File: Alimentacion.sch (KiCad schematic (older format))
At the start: 3 parts

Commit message: version preliminar de la etapa de alimentacion
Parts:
- added C1, C4: 4,7u, symbol C
- added C? (x2): 4u7, symbol C
- added C?: 10u, symbol C
- added D1: LED, symbol LED
- added L?: 4u7, symbol L
- added P1: CONN_01X02, symbol CONN_01X02
- added Q?: NX2301P, symbol NX2301P
- added Q?: BC849, SOT-23, symbol BC849
- added R1, R2: 470, symbol R
- added R? (x2): 10K, symbol R
- added R?: 976K, symbol R
- added R?: 309K, symbol R
- added R?: 47K, symbol R
- added R?: 1K, symbol R
- added U1: MCP73831T, symbol MCP73831T
- added U?: MCP1640, symbol MCP1640
- U2: renamed from U?; footprint SOT-223 -> (none)
- gave numbers to parts that had none: 2
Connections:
- net labels added: +3V3, +5V, V5VBOOST, VBATT, VUSB
- wire segments 8 -> 59
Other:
- moved on the sheet: C2, C3, U2

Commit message: asignacion inicial de huellas
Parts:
- C1, C3, C4: footprint (none) -> Capacitors_SMD:C_1206
- C2: footprint (none) -> Capacitors_SMD:C_0805
- C34, C35, C36: renamed from C?; footprint (none) -> Capacitors_SMD:C_1206
- D1: footprint (none) -> LEDs:LED_0805
- L2: renamed from L?; footprint (none) -> Magneticos:BOURNS_SRN4012T
- P1: footprint (none) -> Connectors_Molex:Molex_PicoBlade_53047-0210_02x1.25mm_Straight
- Q10: renamed from Q?; footprint SOT-23 -> TO_SOT_Packages_SMD:SOT-23
- Q11: renamed from Q?; footprint (none) -> TO_SOT_Packages_SMD:SOT-23
- R1, R2: footprint (none) -> Resistencias:R_0805
- R54, R55, R56, R57, R58, R59: renamed from R?; footprint (none) -> Resistencias:R_0805
- U1: footprint (none) -> TO_SOT_Packages_SMD:SOT-23-5; Fabricante (none) -> MICROCHIP; Provedor (none) -> rs; Ref (none) -> MCP73831T-2ATI/OT; Ref_Proveedor (none) -> 738-6617
- U12: renamed from U?; footprint (none) -> TO_SOT_Packages_SMD:SOT-23-6
- U2: footprint (none) -> TO_SOT_Packages_SMD:SOT-223; Fabricante (none) -> ST; Ref (none) -> LD1117S33TR

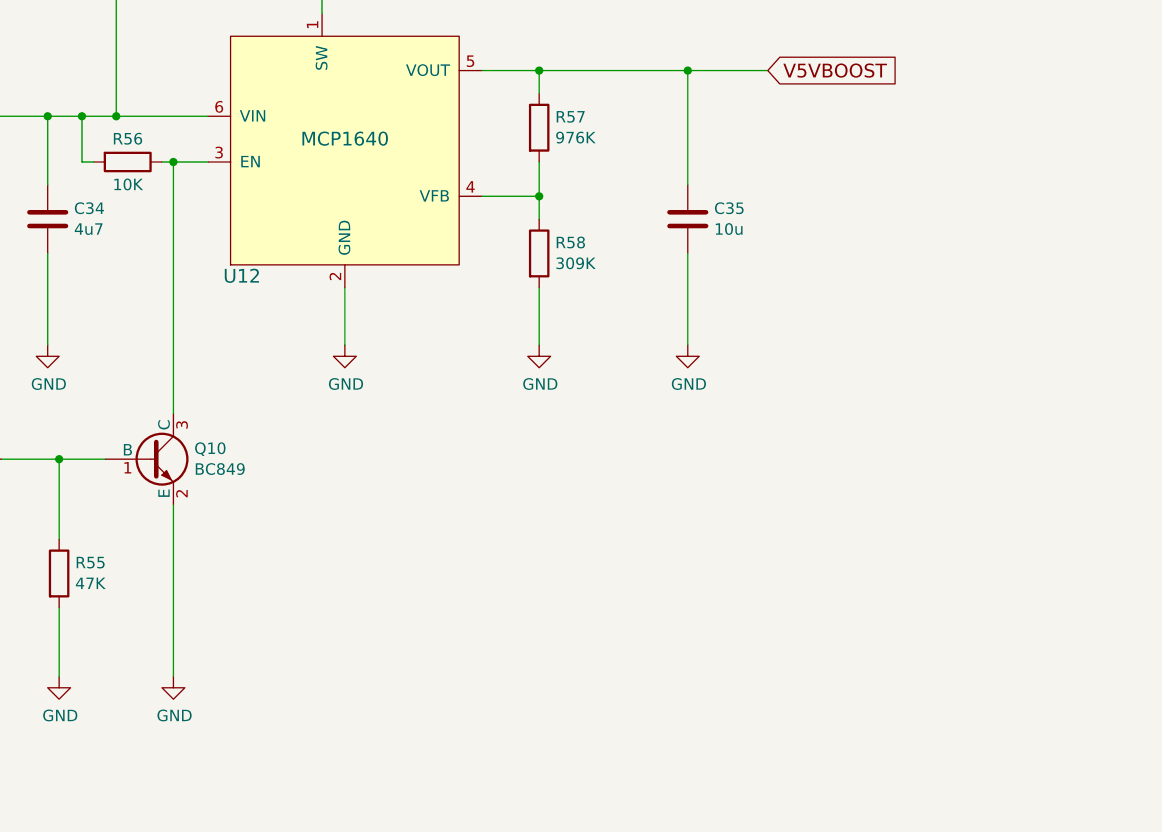
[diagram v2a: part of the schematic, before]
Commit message: cambiar ch340T por ch340g y añadir nc a pines
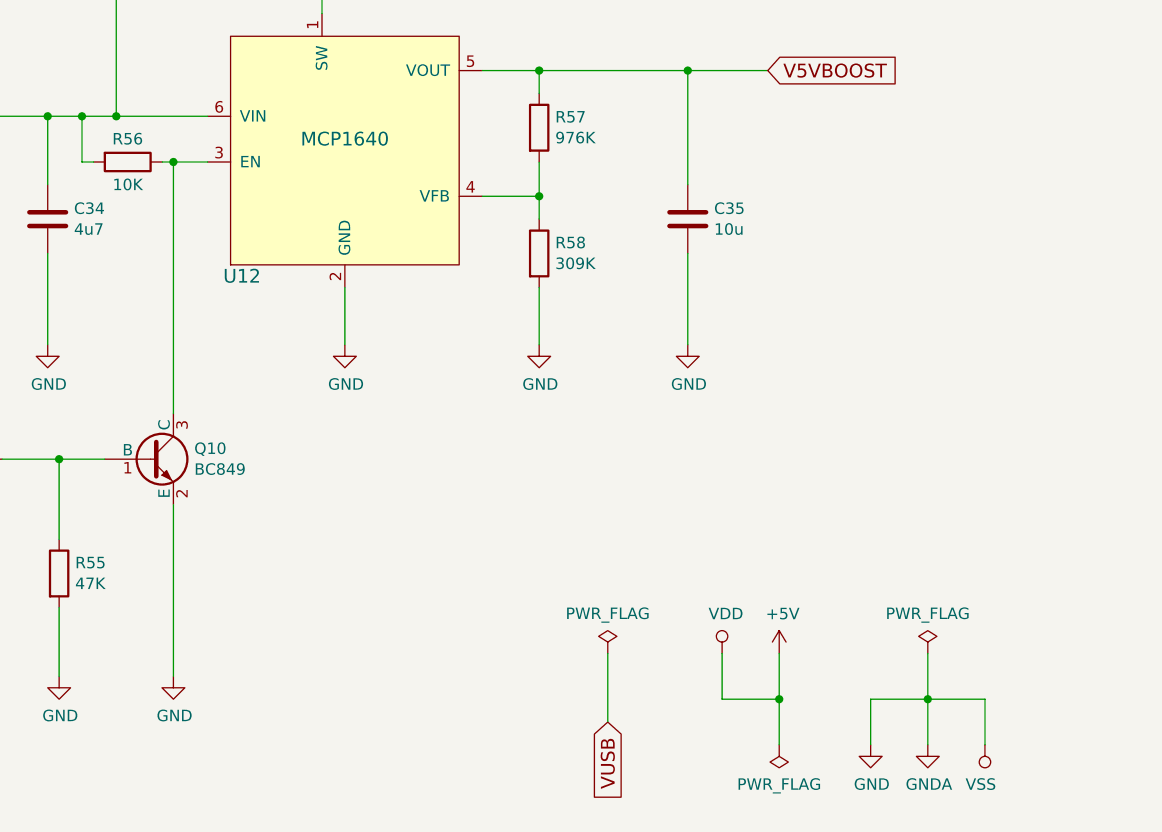
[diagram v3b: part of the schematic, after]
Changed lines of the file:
@@
 $Descr A4 11693 8268
 encoding utf-8
-Sheet 2 15
+Sheet 2 14
 Title "Etapa de Alimentación"
 Date "2017-01-15"
@@
 $EndComp
 Wire Wire Line
-	2900 4450 2700 4450
+	2700 4450 2900 4450
 Wire Wire Line
 	2400 4450 2350 4450
@@
 Wire Wire Line
 	9750 4100 9750 3900
+$Comp
+L PWR_FLAG #FLG016
+U 1 1 589667C8
+P 4650 6600
+F 0 "#FLG016" H 3550 5475 50  0001 C CNN
+F 1 "PWR_FLAG" H 4650 6774 50  0000 C CNN
+F 2 "" H 3550 5400 50  0001 C CNN
+F 3 "" H 3550 5400 50  0001 C CNN
+	1    4650 6600
+	1    0    0    -1
+$EndComp
+Text GLabel 4650 6900 3    60   Input ~ 0
+VUSB
+$Comp
+L +5V #PWR017
+U 1 1 58967CBF
+P 5400 6600
+F 0 "#PWR017" H 5400 6450 50  0001 C CNN
+F 1 "+5V" H 5415 6773 50  0000 C CNN
+F 2 "" H 5400 6600 50  0001 C CNN
+F 3 "" H 5400 6600 50  0001 C CNN
+	1    5400 6600
+	1    0    0    -1
+$EndComp
+$Comp
+L PWR_FLAG #FLG018
+U 1 1 58967D6B
+P 5400 7000
+F 0 "#FLG018" H 4300 5875 50  0001 C CNN
+F 1 "PWR_FLAG" H 5400 7173 50  0000 C CNN
+F 2 "" H 4300 5800 50  0001 C CNN
+F 3 "" H 4300 5800 50  0001 C CNN
+	1    5400 7000
+	-1   0    0    1
+$EndComp
+$Comp
+L GND #PWR019
+U 1 1 58967DD4
+P 5800 7000
+F 0 "#PWR019" H 5850 7050 50  0001 C CNN
+F 1 "GND" H 5805 6827 50  0000 C CNN
+F 2 "" H -100 150 50  0001 C CNN
+F 3 "" H -100 150 50  0001 C CNN
+	1    5800 7000
+	1    0    0    -1
+$EndComp
+$Comp
+L GNDA #PWR020
+U 1 1 58967E16
+P 6050 7000
+F 0 "#PWR020" H 6100 7050 50  0001 C CNN
+F 1 "GNDA" H 6055 6827 50  0000 C CNN
+F 2 "" H 50  0   50  0001 C CNN
+F 3 "" H 50  0   50  0001 C CNN
+	1    6050 7000
+	1    0    0    -1
+$EndComp
+Wire Wire Line
+	6050 6600 6050 7000
+Wire Wire Line
+	5800 6800 6300 6800
+Wire Wire Line
+	5800 6800 5800 7000
+$Comp
+L PWR_FLAG #FLG021
+U 1 1 58967ED4
+P 6050 6600
+F 0 "#FLG021" H 4950 5475 50  0001 C CNN
+F 1 "PWR_FLAG" H 6050 6774 50  0000 C CNN
+F 2 "" H 4950 5400 50  0001 C CNN
+F 3 "" H 4950 5400 50  0001 C CNN
+	1    6050 6600
+	1    0    0    -1
+$EndComp
+Connection ~ 6050 6800
+Wire Wire Line
+	5400 6600 5400 7000
+Wire Wire Line
+	4650 6600 4650 6900
+$Comp
+L VDD #PWR022
+U 1 1 58968AA7
+P 5150 6600
+F 0 "#PWR022" H 5200 6650 50  0001 C CNN
+F 1 "VDD" H 5167 6773 50  0000 C CNN
+F 2 "" H -50 -50 50  0001 C CNN
+F 3 "" H -50 -50 50  0001 C CNN
+	1    5150 6600
+	1    0    0    -1
+$EndComp
+Wire Wire Line
+	5150 6600 5150 6800
+Wire Wire Line
+	5150 6800 5400 6800
+Connection ~ 5400 6800
+$Comp
+L VSS #PWR023
+U 1 1 58968B58
+P 6300 7000
+F 0 "#PWR023" H 6350 7050 50  0001 C CNN
+F 1 "VSS" H 6318 7173 50  0000 C CNN
+F 2 "" H 0   100 50  0001 C CNN
+F 3 "" H 0   100 50  0001 C CNN
+	1    6300 7000
+	-1   0    0    1
+$EndComp
+Wire Wire Line
+	6300 6800 6300 7000
 $EndSCHEMATC

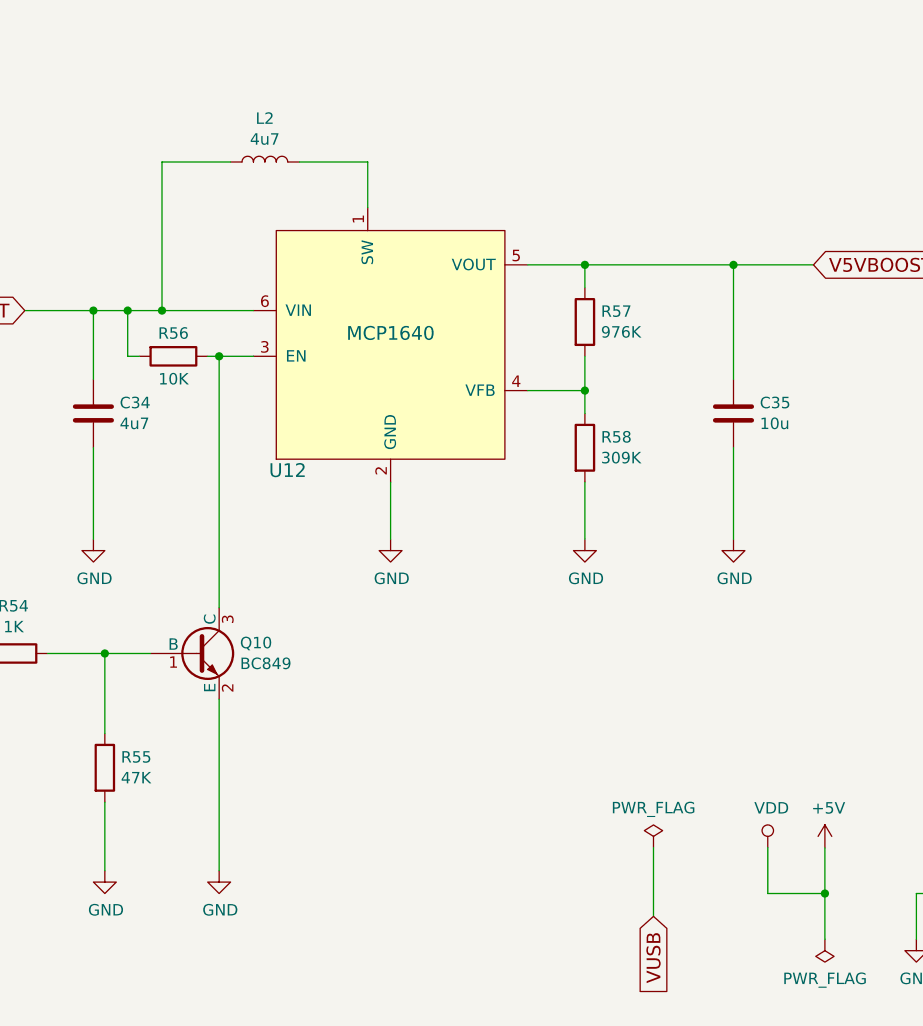
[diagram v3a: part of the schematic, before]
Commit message: cambiado cristal de cuarzo por resonador
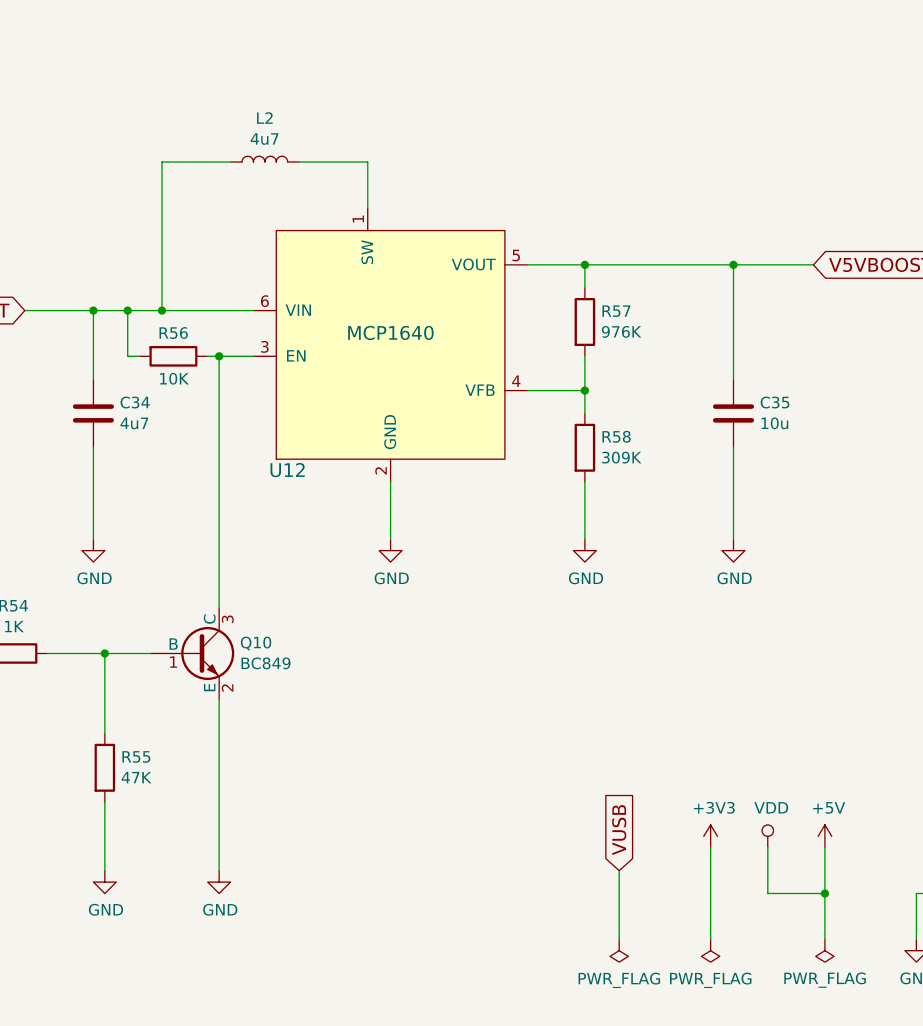
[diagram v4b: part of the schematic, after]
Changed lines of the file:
@@
 	2800 3600 2500 3600
 Wire Wire Line
-	2500 3600 2500 4250
+	2500 4250 2500 3600
 Wire Wire Line
 	1900 4250 2900 4250
@@
 L PWR_FLAG #FLG016
 U 1 1 589667C8
-P 4650 6600
-F 0 "#FLG016" H 3550 5475 50  0001 C CNN
-F 1 "PWR_FLAG" H 4650 6774 50  0000 C CNN
-F 2 "" H 3550 5400 50  0001 C CNN
-F 3 "" H 3550 5400 50  0001 C CNN
-	1    4650 6600
-	1    0    0    -1
-$EndComp
-Text GLabel 4650 6900 3    60   Input ~ 0
+P 4500 7000
+F 0 "#FLG016" H 3400 5875 50  0001 C CNN
+F 1 "PWR_FLAG" H 4500 7174 50  0000 C CNN
+F 2 "" H 3400 5800 50  0001 C CNN
+F 3 "" H 3400 5800 50  0001 C CNN
+	1    4500 7000
+	-1   0    0    1
+$EndComp
+Text GLabel 4500 6700 1    60   Input ~ 0
 VUSB
 $Comp
@@
 	5400 6600 5400 7000
 Wire Wire Line
-	4650 6600 4650 6900
+	4500 7000 4500 6700
 $Comp
 L VDD #PWR022
@@
 Wire Wire Line
 	6300 6800 6300 7000
+$Comp
+L +3V3 #PWR024
+U 1 1 58967A37
+P 4900 6600
+F 0 "#PWR024" H 4950 6650 50  0001 C CNN
+F 1 "+3V3" H 4915 6773 50  0000 C CNN
+F 2 "" H -1400 -150 50  0001 C CNN
+F 3 "" H -1400 -150 50  0001 C CNN
+	1    4900 6600
+	1    0    0    -1
+$EndComp
+$Comp
+L PWR_FLAG #FLG025
+U 1 1 58967A8E
+P 4900 7000
+F 0 "#FLG025" H 3800 5875 50  0001 C CNN
+F 1 "PWR_FLAG" H 4900 7174 50  0000 C CNN
+F 2 "" H 3800 5800 50  0001 C CNN
+F 3 "" H 3800 5800 50  0001 C CNN
+	1    4900 7000
+	-1   0    0    1
+$EndComp
+Wire Wire Line
+	4900 6600 4900 7000
 $EndSCHEMATC

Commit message: place inicial sobre la pcb
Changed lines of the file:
@@
 	2800 3600 2500 3600
 Wire Wire Line
-	2500 4250 2500 3600
+	2500 3600 2500 4250
 Wire Wire Line
 	1900 4250 2900 4250
@@
 L PWR_FLAG #FLG016
 U 1 1 589667C8
-P 4500 7000
-F 0 "#FLG016" H 3400 5875 50  0001 C CNN
-F 1 "PWR_FLAG" H 4500 7174 50  0000 C CNN
-F 2 "" H 3400 5800 50  0001 C CNN
-F 3 "" H 3400 5800 50  0001 C CNN
-	1    4500 7000
+P 4850 7000
+F 0 "#FLG016" H 3750 5875 50  0001 C CNN
+F 1 "PWR_FLAG" H 4850 7174 50  0000 C CNN
+F 2 "" H 3750 5800 50  0001 C CNN
+F 3 "" H 3750 5800 50  0001 C CNN
+	1    4850 7000
 	-1   0    0    1
 $EndComp
-Text GLabel 4500 6700 1    60   Input ~ 0
+Text GLabel 4850 6700 1    60   Input ~ 0
 VUSB
 $Comp
@@
 	5400 6600 5400 7000
 Wire Wire Line
-	4500 7000 4500 6700
+	4850 7000 4850 6700
 $Comp
 L VDD #PWR022
@@
 Wire Wire Line
 	6300 6800 6300 7000
-$Comp
-L +3V3 #PWR024
-U 1 1 58967A37
-P 4900 6600
-F 0 "#PWR024" H 4950 6650 50  0001 C CNN
-F 1 "+3V3" H 4915 6773 50  0000 C CNN
-F 2 "" H -1400 -150 50  0001 C CNN
-F 3 "" H -1400 -150 50  0001 C CNN
-	1    4900 6600
-	1    0    0    -1
-$EndComp
-$Comp
-L PWR_FLAG #FLG025
-U 1 1 58967A8E
-P 4900 7000
-F 0 "#FLG025" H 3800 5875 50  0001 C CNN
-F 1 "PWR_FLAG" H 4900 7174 50  0000 C CNN
-F 2 "" H 3800 5800 50  0001 C CNN
-F 3 "" H 3800 5800 50  0001 C CNN
-	1    4900 7000
-	-1   0    0    1
-$EndComp
-Wire Wire Line
-	4900 6600 4900 7000
 $EndSCHEMATC

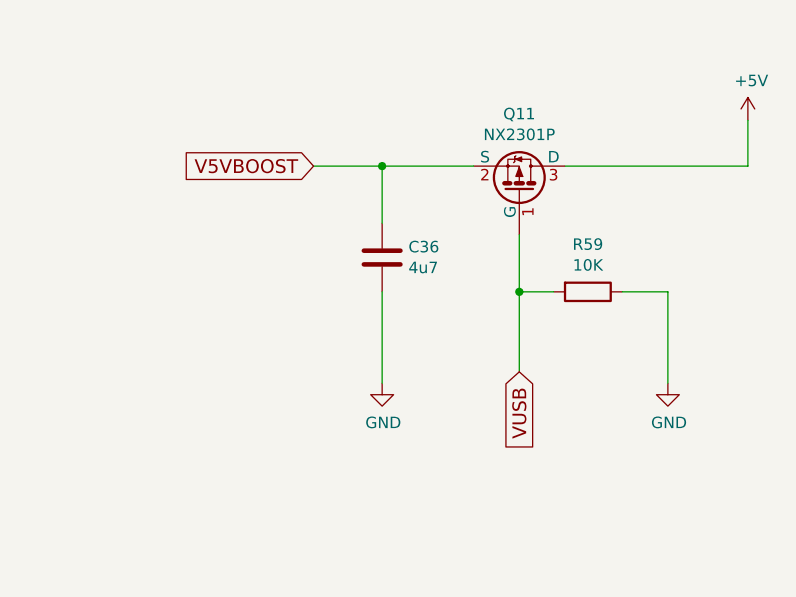
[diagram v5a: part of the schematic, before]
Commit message: ordenar componentes y referencias
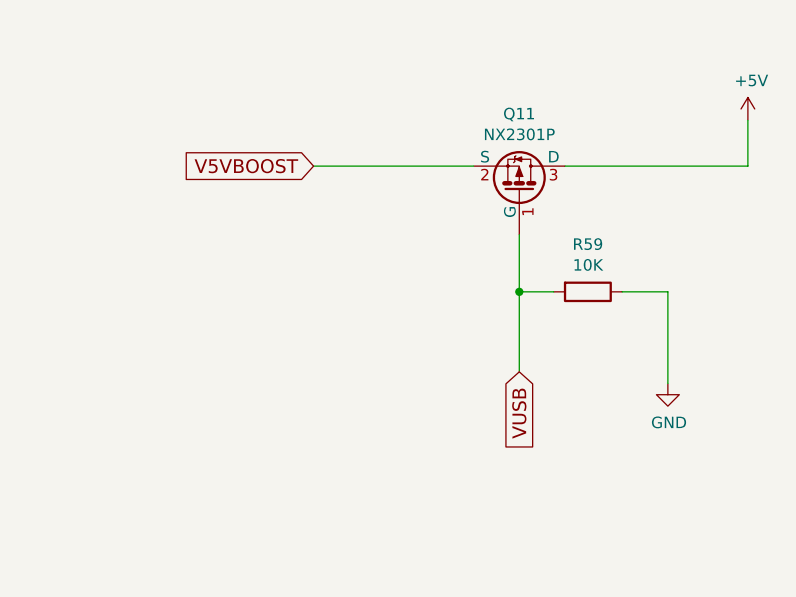
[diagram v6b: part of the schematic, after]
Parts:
- removed C36: 4u7, Capacitors_SMD:C_1206, symbol C
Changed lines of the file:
@@
 	1    0    0    -1
 $EndComp
-$Comp
-L C C36
-U 1 1 588F763A
-P 8150 4500
-F 0 "C36" H 8265 4546 50  0000 L CNN
-F 1 "4u7" H 8265 4455 50  0000 L CNN
-F 2 "Capacitors_SMD:C_1206" H 8188 4350 50  0001 C CNN
-F 3 "" H 8150 4500 50  0001 C CNN
-	1    8150 4500
-	1    0    0    -1
-$EndComp
-$Comp
-L GND #PWR08
-U 1 1 588F7687
-P 8150 5050
-F 0 "#PWR08" H 8150 4800 50  0001 C CNN
-F 1 "GND" H 8155 4877 50  0000 C CNN
-F 2 "" H 8150 5050 50  0001 C CNN
-F 3 "" H 8150 5050 50  0001 C CNN
-	1    8150 5050
-	1    0    0    -1
-$EndComp
-Wire Wire Line
-	8150 5050 8150 4650
-Wire Wire Line
-	8150 4350 8150 4100
-Connection ~ 8150 4100
 Text GLabel 8750 5000 3    60   Input ~ 0
 VUSB
@@
 	4350 5250 4350 5000
 $Comp
-L GND #PWR09
+L GND #PWR08
 U 1 1 588FCE2A
 P 4350 5250
-F 0 "#PWR09" H 4350 5000 50  0001 C CNN
+F 0 "#PWR08" H 4350 5000 50  0001 C CNN
 F 1 "GND" H 4355 5077 50  0000 C CNN
 F 2 "" H 4350 5250 50  0001 C CNN
@@
 $EndComp
 $Comp
-L GND #PWR010
+L GND #PWR09
 U 1 1 588FCE72
 P 3500 5250
-F 0 "#PWR010" H 3500 5000 50  0001 C CNN
+F 0 "#PWR09" H 3500 5000 50  0001 C CNN
 F 1 "GND" H 3505 5077 50  0000 C CNN
 F 2 "" H 3500 5250 50  0001 C CNN
@@
 $EndComp
 $Comp
-L GND #PWR011
+L GND #PWR010
 U 1 1 588FCF31
 P 2200 5250
-F 0 "#PWR011" H 2200 5000 50  0001 C CNN
+F 0 "#PWR010" H 2200 5000 50  0001 C CNN
 F 1 "GND" H 2205 5077 50  0000 C CNN
 F 2 "" H 2200 5250 50  0001 C CNN
@@
 Connection ~ 4350 4050
 $Comp
-L GND #PWR012
+L GND #PWR011
 U 1 1 588FD427
 P 5000 5250
-F 0 "#PWR012" H 5000 5000 50  0001 C CNN
+F 0 "#PWR011" H 5000 5000 50  0001 C CNN
 F 1 "GND" H 5005 5077 50  0000 C CNN
 F 2 "" H 5000 5250 50  0001 C CNN
@@
 	2750 5950 2750 6700
 $Comp
-L GND #PWR013
+L GND #PWR012
 U 1 1 588FEB50
 P 2750 6700
-F 0 "#PWR013" H 2750 6450 50  0001 C CNN
+F 0 "#PWR012" H 2750 6450 50  0001 C CNN
 F 1 "GND" H 2755 6527 50  0000 C CNN
 F 2 "" H 2750 6700 50  0001 C CNN
@@
 $EndComp
 $Comp
-L GND #PWR014
+L GND #PWR013
 U 1 1 588FEBE6
 P 2250 6700
-F 0 "#PWR014" H 2250 6450 50  0001 C CNN
+F 0 "#PWR013" H 2250 6450 50  0001 C CNN
 F 1 "GND" H 2255 6527 50  0000 C CNN
 F 2 "" H 2250 6700 50  0001 C CNN
@@
 VUSB
 $Comp
-L +5V #PWR015
+L +5V #PWR014
 U 1 1 588FF39A
 P 9750 3900
-F 0 "#PWR015" H 9750 3750 50  0001 C CNN
+F 0 "#PWR014" H 9750 3750 50  0001 C CNN
 F 1 "+5V" H 9765 4073 50  0000 C CNN
 F 2 "" H 9750 3900 50  0001 C CNN
@@
 	9750 4100 9750 3900
 $Comp
-L PWR_FLAG #FLG016
+L PWR_FLAG #FLG015
 U 1 1 589667C8
 P 4850 7000
-F 0 "#FLG016" H 3750 5875 50  0001 C CNN
+F 0 "#FLG015" H 3750 5875 50  0001 C CNN
 F 1 "PWR_FLAG" H 4850 7174 50  0000 C CNN
 F 2 "" H 3750 5800 50  0001 C CNN
@@
 VUSB
 $Comp
-L +5V #PWR017
+L +5V #PWR016
 U 1 1 58967CBF
 P 5400 6600
-F 0 "#PWR017" H 5400 6450 50  0001 C CNN
+F 0 "#PWR016" H 5400 6450 50  0001 C CNN
 F 1 "+5V" H 5415 6773 50  0000 C CNN
 F 2 "" H 5400 6600 50  0001 C CNN
@@
 $EndComp
 $Comp
-L PWR_FLAG #FLG018
+L PWR_FLAG #FLG017
 U 1 1 58967D6B
 P 5400 7000
-F 0 "#FLG018" H 4300 5875 50  0001 C CNN
+F 0 "#FLG017" H 4300 5875 50  0001 C CNN
 F 1 "PWR_FLAG" H 5400 7173 50  0000 C CNN
 F 2 "" H 4300 5800 50  0001 C CNN
@@
 $EndComp
 $Comp
-L GND #PWR019
+L GND #PWR018
 U 1 1 58967DD4
 P 5800 7000
-F 0 "#PWR019" H 5850 7050 50  0001 C CNN
+F 0 "#PWR018" H 5850 7050 50  0001 C CNN
 F 1 "GND" H 5805 6827 50  0000 C CNN
 F 2 "" H -100 150 50  0001 C CNN
@@
 $EndComp
 $Comp
-L GNDA #PWR020
+L GNDA #PWR019
 U 1 1 58967E16
 P 6050 7000
-F 0 "#PWR020" H 6100 7050 50  0001 C CNN
+F 0 "#PWR019" H 6100 7050 50  0001 C CNN
 F 1 "GNDA" H 6055 6827 50  0000 C CNN
 F 2 "" H 50  0   50  0001 C CNN
@@
 	5800 6800 5800 7000
 $Comp
-L PWR_FLAG #FLG021
+L PWR_FLAG #FLG020
 U 1 1 58967ED4
 P 6050 6600
-F 0 "#FLG021" H 4950 5475 50  0001 C CNN
+F 0 "#FLG020" H 4950 5475 50  0001 C CNN
 F 1 "PWR_FLAG" H 6050 6774 50  0000 C CNN
 F 2 "" H 4950 5400 50  0001 C CNN
@@
 	4850 7000 4850 6700
 $Comp
-L VDD #PWR022
+L VDD #PWR021
 U 1 1 58968AA7
 P 5150 6600
-F 0 "#PWR022" H 5200 6650 50  0001 C CNN
+F 0 "#PWR021" H 5200 6650 50  0001 C CNN
 F 1 "VDD" H 5167 6773 50  0000 C CNN
 F 2 "" H -50 -50 50  0001 C CNN
@@
 Connection ~ 5400 6800
 $Comp
-L VSS #PWR023
+L VSS #PWR022
 U 1 1 58968B58
 P 6300 7000
-F 0 "#PWR023" H 6350 7050 50  0001 C CNN
+F 0 "#PWR022" H 6350 7050 50  0001 C CNN
 F 1 "VSS" H 6318 7173 50  0000 C CNN
 F 2 "" H 0   100 50  0001 C CNN
